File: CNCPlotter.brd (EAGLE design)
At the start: 112.4 x 73.7 mm, 126 parts, among them IC1 HEF4050B, IC2 MC34063, IC3 LD111733, IC4 74HC4094, IC5 ATmega32U4, IC6 DRV8811, IC7 DRV8811, J1 Servo, J10 Touchscreen, J11 Touchscreen, J12 X Motor, J13 MS1, J14 MS0, J15 Y Motor, J16 MS1, J17 MS0, J2 Z Drive, J3 ISP, J4 UART, J5 12V Supply, J6 MicroSD Card, J7 HWB, J8 USB, J9 Home Switches, Q1 16MHz

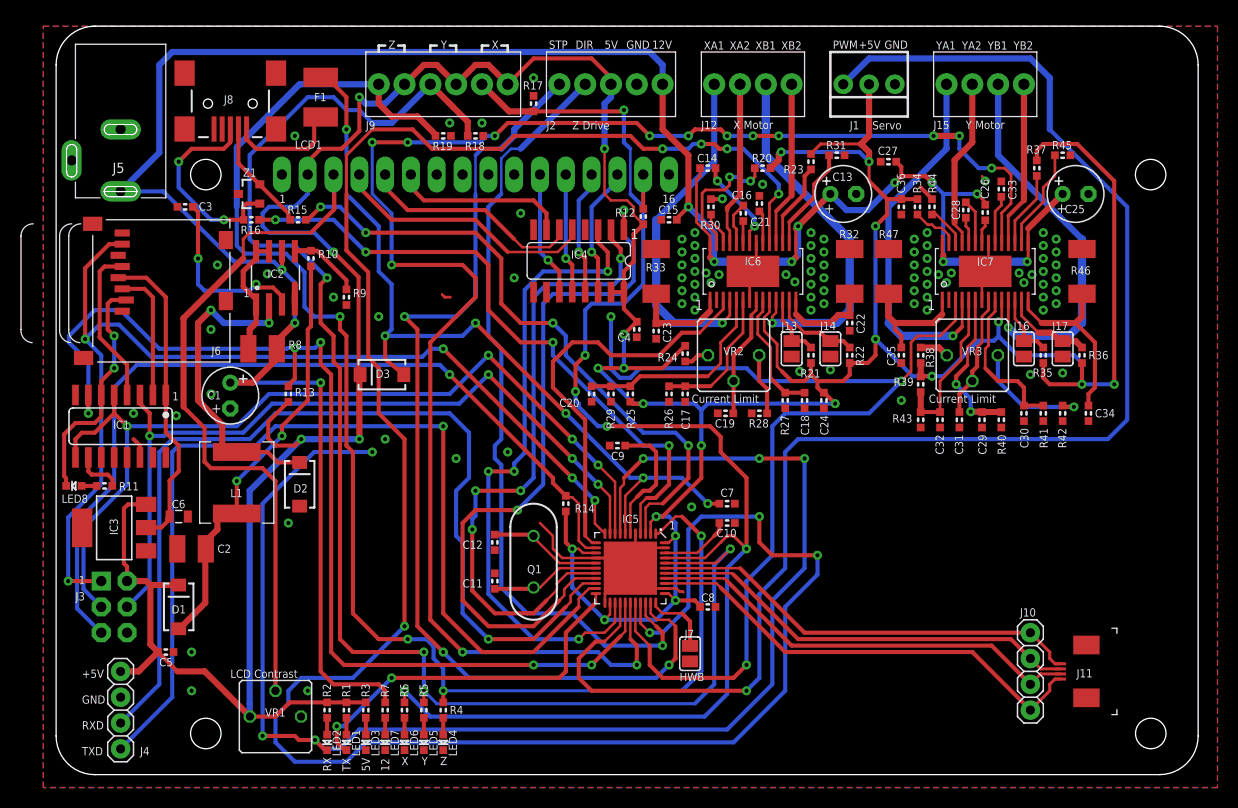
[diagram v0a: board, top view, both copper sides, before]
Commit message: Removed CNCPlotter files
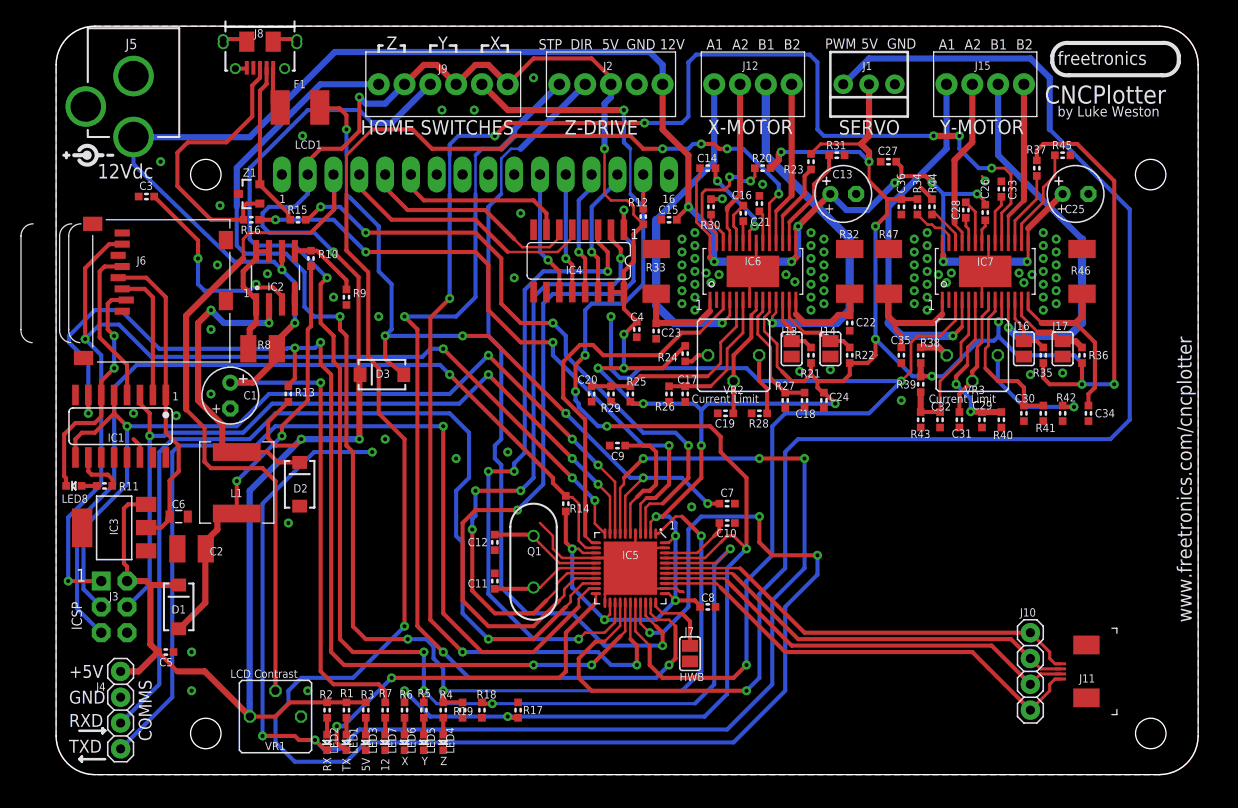
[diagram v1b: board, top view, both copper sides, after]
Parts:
- J1: value Servo -> SERVO
- J12: value X Motor -> X-MOTOR
- J15: value Y Motor -> Y-MOTOR
- J2: value Z Drive -> Z-DRIVE
- J5: device SparkFun:POWER_JACK_SLOT -> freetronics-master-v1.1:POWER_JACK_PTH
- J8: value USB -> USB-6PSMT; device freetronics-luke:USB-MINIB-FT -> freetronics-jon:USB-MICROB-MB05PMXX
- moved R17 59.7 mm to (45.5, 6.35)
- moved R19 56.5 mm to (40.0, 6.35), turned to 270 degrees
- moved R18 56.5 mm to (41.9, 6.35), turned to 270 degrees
- moved J5 13.0 mm to (7.62, 76.5)
- moved J8 5.64 mm to (20.1, 72.1), turned to 180 degrees
- moved C3 3.94 mm to (8.89, 56.9)
- moved F1 2.27 mm to (24.0, 65.7), turned to 0 degrees
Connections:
- net GND: now also J5.GNDBREAK, J8.FIX1, J8.FIX2, J8.PIN1, J8.PIN2, J8.TAB1, J8.TAB2; no longer J8.SH1, J8.SH2, J8.SH3, J8.SH4
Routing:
- net Z_HOME: track 149.3 -> 133.1 mm
- net N$2: track 12.6 -> 4.41 mm
- net N$33: track 20.7 -> 28.4 mm, vias 2 -> 0
- net Y_HOME: track 148.2 -> 140.9 mm, vias 4 -> 5
- net +12V: track 244.9 -> 238.8 mm
- net GND: track 52.5 -> 58.4 mm, vias 93 -> 95
- net N$34: track 11.2 -> 16.6 mm
- net Y_STEP: track 159.8 -> 154.8 mm, vias 14 -> 8
- net N$40: track 82.0 -> 78.8 mm
- net N$43: track 17.9 -> 20.5 mm
- net X_DIR: track 44.6 -> 43.0 mm
- net X_HOME: track 136.9 -> 138.1 mm, vias 6 -> 7
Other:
- board text added: "(C) 2012 Luke Weston"
- board text added: "12Vdc"
- board text added: "A1"
- board text added: "A2"
- board text added: "Arduino-compatible"
- board text added: "B1"
- board text added: "B2"
- board text added: "CNC Plotter Controller"
- board text added: "CNCPlotter"
- board text added: "COMMS"
- board text added: "HOME SWITCHES"
- board text added: "Hardware License:"
- board text added: "ICSP"
- board text added: "Released under"
- board text added: "SKU: CNCPLOT"
- board text added: "V1.0"
- board text added: "by Luke Weston"
- board text added: "freetronics"
- board text added: "the TAPR Open"
- board text added: "www.freetronics.com/cncplotter"
- board text added: "www.tapr.org/OHL"
- board text removed: "XA1"
- board text removed: "XA2"
- board text removed: "XB1"
- board text removed: "XB2"
- board text removed: "YA1"
- board text removed: "YA2"
- board text removed: "YB1"
- board text removed: "YB2"
